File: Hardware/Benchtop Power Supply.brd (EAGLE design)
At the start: 114.3 x 48.3 mm, 20 parts, among them J1 ATX24RH

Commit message: Midway hardware changes
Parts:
- added FRAME1: FRAME-LETTER, SparkFun-Aesthetics:CREATIVE_COMMONS
- added S9: (no value), SparkFun-Electromechanical:SWITCH-SPDT_KIT
- added U$1: REVISION, SparkFun-Aesthetics:REVISION
- J1: device SparkFun:ATX24_RIGHT_ANGLE -> SparkFun-Connectors:ATX24_RIGHT_ANGLE
- moved JP1 84.8 mm to (3.94, 15.6)
- moved S8 21.6 mm to (123.2, 38.1)
- moved F4 19.0 mm to (114.3, 26.7)
- moved JP2 17.8 mm to (129.5, 2.54)
- moved JP3 17.8 mm to (129.5, 45.7)
- moved S6 15.2 mm to (91.4, 38.1)
- moved S7 15.2 mm to (104.1, 38.1)
- moved F3 12.7 mm to (82.5, 26.7)
- moved J1 8.89 mm to (66.0, 8.89)
- moved S4 8.89 mm to (59.7, 38.1)
- moved S5 8.89 mm to (72.4, 38.1)
- moved F1 5.08 mm to (49.5, 26.7)
- moved LED1 3.81 mm to (27.9, 6.35)
- moved R1 3.81 mm to (27.9, 11.4)
- moved S1 3.81 mm to (8.89, 38.1)
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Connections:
- new net N$2: J1.16, S9.2
- net GND: now also S9.3; no longer J1.16
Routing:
- net 3.3V: track 74.7 -> 0.00 mm
- net 5V: track 64.8 -> 0.00 mm
- net 12V: track 31.4 -> 0.00 mm
- net 5V_P: track 15.2 -> 1.35 mm
- net -12V: track 11.0 -> 0.00 mm
- net 3.3V_P: track 9.93 -> 0.95 mm
- net -12V_P: track 8.32 -> 0.00 mm
- net 12V_P: track 8.32 -> 0.00 mm
- net N$1: track 6.13 -> 0.00 mm
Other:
- board size 114.3 x 48.3 mm -> 132.1 x 48.3 mm
- board text added: "Ryan Owens"
- board text added: "Toni Klopfenstein"
- board text added: "V13"
- board text removed: "3/29/10"

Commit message: Files changed for V13- ready for review
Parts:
- added LOGO1: OSHW-LOGOL, SparkFun-Aesthetics:OSHW-LOGO-L
- JP1: value LOGO-SFENEW -> SFE_LOGO_NAME_FLAME.3_INCH; device SparkFun:SFE-NEW-WEBLOGO -> SparkFun-Aesthetics:SFE_LOGO_NAME_FLAME_.3
- moved JP1 93.1 mm to (96.6, 6.73)
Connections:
- new net NC: S9.1
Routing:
- net 3.3V: track 0.00 -> 76.0 mm
- net 5V: track 0.00 -> 67.3 mm
- net N$2: track 0.00 -> 37.2 mm
- net 12V: track 0.00 -> 32.4 mm
- net -12V: track 0.00 -> 22.0 mm
- net 5V_P: track 1.35 -> 18.8 mm
- net 3.3V_P: track 0.95 -> 13.2 mm
- net 12V_P: track 0.00 -> 7.27 mm
- net -12V_P: track 0.00 -> 7.27 mm
- net N$1: track 0.00 -> 6.88 mm
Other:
- board text added: "Off"
- board text added: "On"

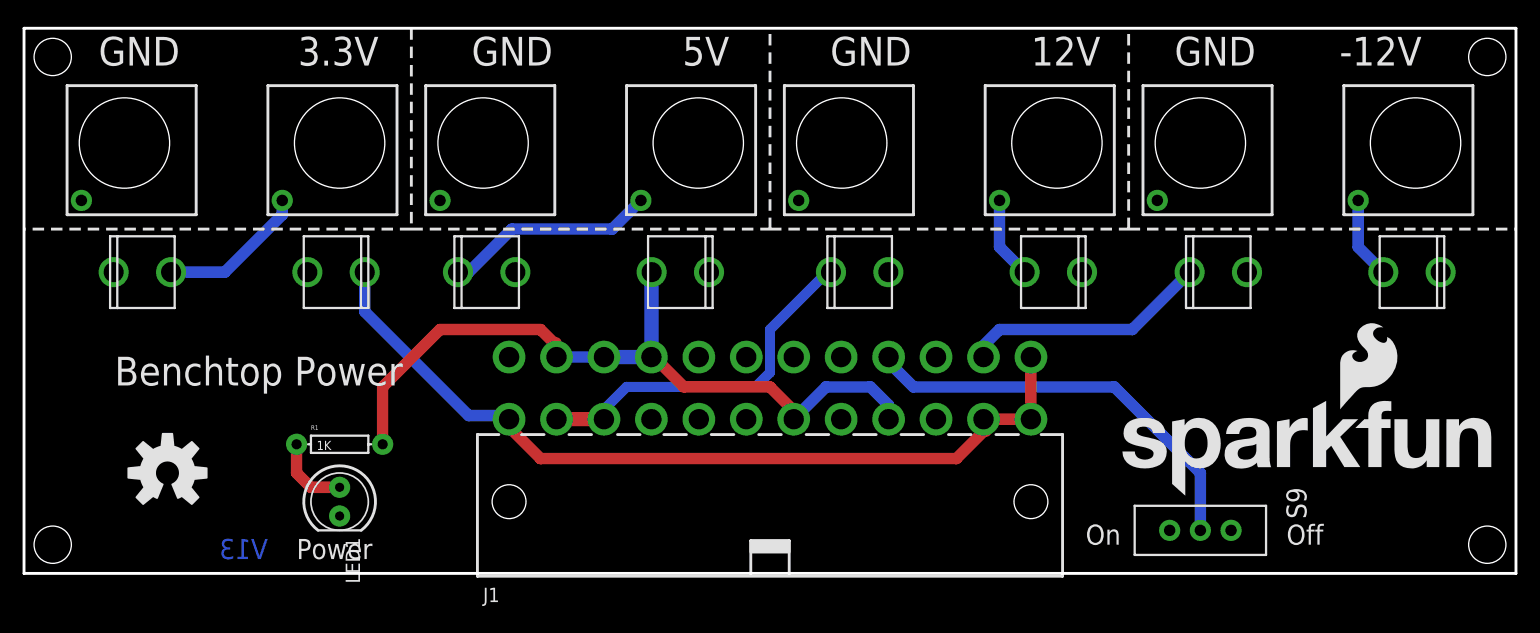
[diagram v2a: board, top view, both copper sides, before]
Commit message: Adding rounded corners, square binding post holes, increased traces to 60 mil
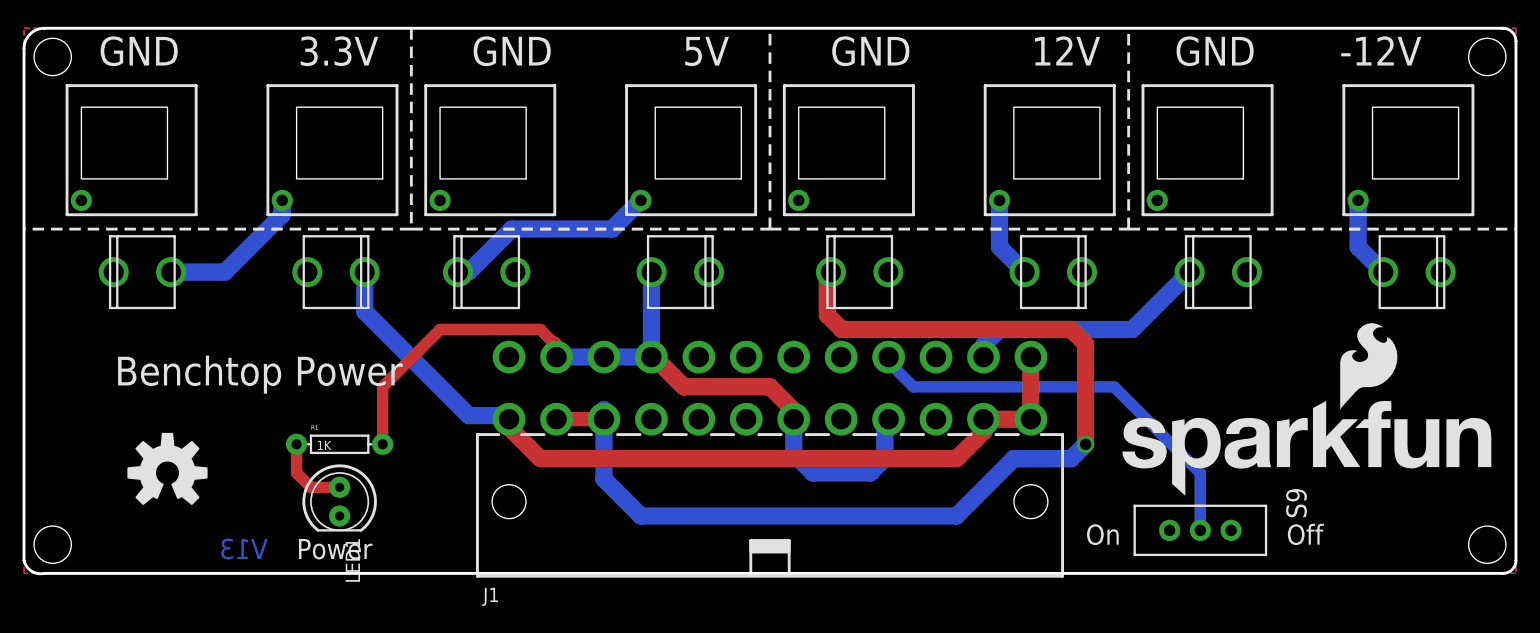
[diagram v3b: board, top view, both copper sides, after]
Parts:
- S1, S2, S3, S4, S5, S6, S7, S8: device SparkFun:BINDING_POST -> SparkFun-Connectors:BINDING_POST
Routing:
- net 12V: track 32.4 -> 95.1 mm, vias 0 -> 1
- net 5V: track 67.3 -> 71.7 mm
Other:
- outline, holes or cut-outs redrawn

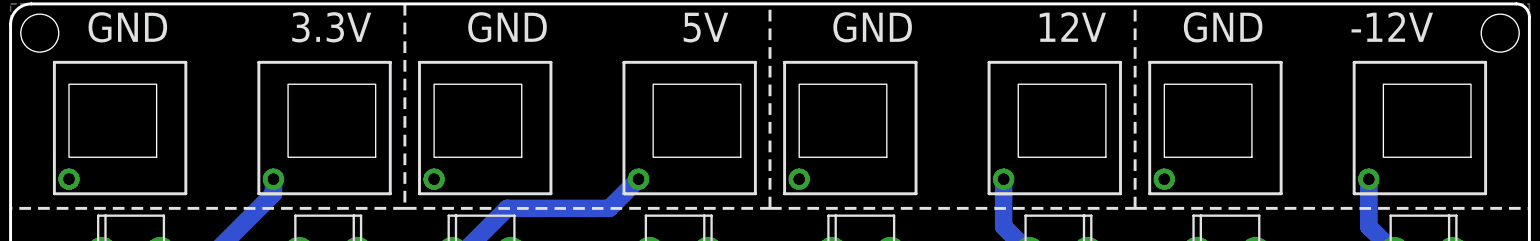
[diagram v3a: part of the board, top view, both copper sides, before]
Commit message: Fixing drill holes for mounting posts
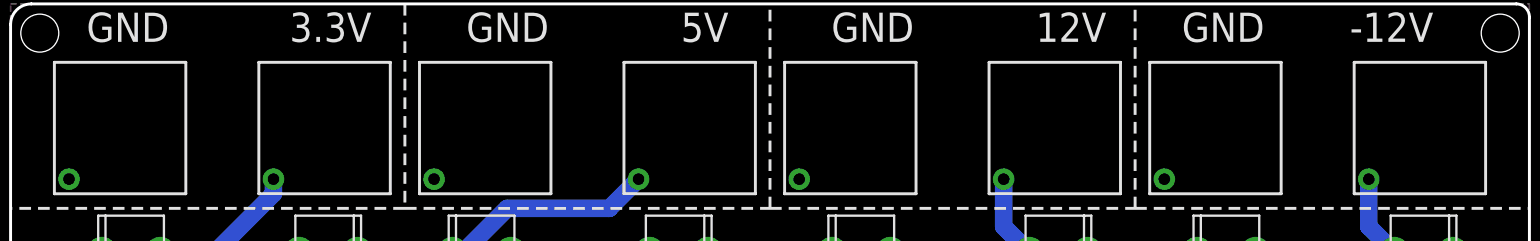
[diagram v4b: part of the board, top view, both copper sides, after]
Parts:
- JP2, JP3, JP4, JP5: device SparkFun:STAND-OFF -> SparkFun-Electromechanical:STAND-OFF
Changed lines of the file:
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@@
 <grid distance="0.05" unitdist="inch" unit="inch" style="lines" multiple="1" display="yes" altdistance="0.005" altunitdist="inch" altunit="inch"/>
 <layers>
-<layer number="1" name="Top" color="4" fill="1" visible="no" active="yes"/>
+<layer number="1" name="Top" color="4" fill="1" visible="yes" active="yes"/>
 <layer number="2" name="Route2" color="1" fill="3" visible="no" active="no"/>
 <layer number="3" name="Route3" color="4" fill="3" visible="no" active="no"/>
@@
 <layer number="14" name="Route14" color="1" fill="6" visible="no" active="no"/>
 <layer number="15" name="Route15" color="4" fill="6" visible="no" active="no"/>
-<layer number="16" name="Bottom" color="1" fill="1" visible="no" active="yes"/>
+<layer number="16" name="Bottom" color="1" fill="1" visible="yes" active="yes"/>
 <layer number="17" name="Pads" color="2" fill="1" visible="yes" active="yes"/>
 <layer number="18" name="Vias" color="2" fill="1" visible="yes" active="yes"/>
@@
 <layer number="46" name="Milling" color="3" fill="1" visible="no" active="yes"/>
 <layer number="47" name="Measures" color="7" fill="1" visible="no" active="yes"/>
-<layer number="48" name="Document" color="7" fill="1" visible="no" active="yes"/>
-<layer number="49" name="Reference" color="7" fill="1" visible="no" active="yes"/>
+<layer number="48" name="Document" color="7" fill="1" visible="yes" active="yes"/>
+<layer number="49" name="Reference" color="7" fill="1" visible="yes" active="yes"/>
 <layer number="50" name="dxf" color="7" fill="1" visible="no" active="yes"/>
 <layer number="51" name="tDocu" color="6" fill="1" visible="yes" active="yes"/>
@@
 <layer number="54" name="bGND_GNDA" color="1" fill="9" visible="no" active="no"/>
 <layer number="56" name="wert" color="7" fill="1" visible="no" active="yes"/>
+<layer number="57" name="tCAD" color="7" fill="1" visible="no" active="no"/>
 <layer number="91" name="Nets" color="2" fill="1" visible="no" active="no"/>
 <layer number="92" name="Busses" color="1" fill="1" visible="no" active="no"/>
@@
 <layer number="97" name="Info" color="7" fill="1" visible="no" active="no"/>
 <layer number="98" name="Guide" color="6" fill="1" visible="no" active="no"/>
+<layer number="99" name="SpiceOrder" color="7" fill="1" visible="no" active="no"/>
 <layer number="100" name="Muster" color="7" fill="1" visible="no" active="no"/>
 <layer number="101" name="Patch_Top" color="12" fill="4" visible="no" active="yes"/>
@@
 <layer number="132" name="bAdjust" color="7" fill="1" visible="no" active="yes"/>
 <layer number="144" name="Drill_legend" color="7" fill="1" visible="no" active="yes"/>
+<layer number="150" name="Notes" color="7" fill="1" visible="yes" active="yes"/>
 <layer number="151" name="HeatSink" color="7" fill="1" visible="no" active="yes"/>
 <layer number="152" name="_bDocu" color="7" fill="1" visible="no" active="yes"/>
+<layer number="153" name="FabDoc1" color="7" fill="1" visible="yes" active="yes"/>
+<layer number="154" name="FabDoc2" color="7" fill="1" visible="yes" active="yes"/>
+<layer number="155" name="FabDoc3" color="7" fill="1" visible="yes" active="yes"/>
 <layer number="199" name="Contour" color="7" fill="1" visible="no" active="yes"/>
 <layer number="200" name="200bmp" color="1" fill="10" visible="no" active="yes"/>
@@
 <elements>
 <element name="JP1" library="SparkFun-Aesthetics" package="SFE_LOGO_NAME_FLAME_.3" value="SFE_LOGO_NAME_FLAME.3_INCH" x="96.647" y="6.731"/>
-<element name="JP2" library="SparkFun" package="STAND-OFF" value="STAND-OFF" x="129.54" y="2.54"/>
-<element name="JP3" library="SparkFun" package="STAND-OFF" value="STAND-OFF" x="129.54" y="45.72"/>
-<element name="JP4" library="SparkFun" package="STAND-OFF" value="STAND-OFF" x="2.54" y="2.54"/>
-<element name="JP5" library="SparkFun" package="STAND-OFF" value="STAND-OFF" x="2.54" y="45.72"/>
+<element name="JP2" library="SparkFun-Electromechanical" package="STAND-OFF" value="STAND-OFF" x="129.54" y="2.54"/>
+<element name="JP3" library="SparkFun-Electromechanical" package="STAND-OFF" value="STAND-OFF" x="129.54" y="45.72"/>
+<element name="JP4" library="SparkFun-Electromechanical" package="STAND-OFF" value="STAND-OFF" x="2.54" y="2.54"/>
+<element name="JP5" library="SparkFun-Electromechanical" package="STAND-OFF" value="STAND-OFF" x="2.54" y="45.72"/>
 <element name="J1" library="SparkFun-Connectors" package="ATX24_RIGHT_ANGLE" value="ATX24RH" x="66.04" y="8.89"/>
 <element name="F1" library="SparkFun" package="FUSE_5MM" value="FUSEX20MM" x="49.53" y="26.67" rot="R270"/>

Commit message: Updating to new binding post footprint
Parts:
- turned S1 to 225 degrees
- turned S2 to 135 degrees
- turned S3 to 225 degrees
- turned S4 to 135 degrees
- turned S5 to 225 degrees
- turned S6 to 135 degrees
- turned S7 to 225 degrees
- turned S8 to 135 degrees
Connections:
- net -12V_P: now also S8.P$1
- net 12V_P: now also S6.P$1
- net 3.3V_P: now also S2.P$1
- net 5V_P: now also S4.P$1
- net GND: now also S1.P$1, S3.P$1, S5.P$1, S7.P$1
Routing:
- net 3.3V_P: track 13.2 -> 13.7 mm, vias 1 -> 0
- net 12V_P: track 7.27 -> 7.71 mm, vias 1 -> 0
- net -12V_P: track 7.27 -> 7.71 mm, vias 1 -> 0
- net 5V_P: vias 1 -> 0
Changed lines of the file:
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@@
 <layer number="46" name="Milling" color="3" fill="1" visible="no" active="yes"/>
 <layer number="47" name="Measures" color="7" fill="1" visible="no" active="yes"/>
-<layer number="48" name="Document" color="7" fill="1" visible="yes" active="yes"/>
-<layer number="49" name="Reference" color="7" fill="1" visible="yes" active="yes"/>
+<layer number="48" name="Document" color="7" fill="1" visible="no" active="yes"/>
+<layer number="49" name="Reference" color="7" fill="1" visible="no" active="yes"/>
 <layer number="50" name="dxf" color="7" fill="1" visible="no" active="yes"/>
 <layer number="51" name="tDocu" color="6" fill="1" visible="yes" active="yes"/>
@@
 <layer number="132" name="bAdjust" color="7" fill="1" visible="no" active="yes"/>
 <layer number="144" name="Drill_legend" color="7" fill="1" visible="no" active="yes"/>
-<layer number="150" name="Notes" color="7" fill="1" visible="yes" active="yes"/>
+<layer number="150" name="Notes" color="7" fill="1" visible="no" active="yes"/>
 <layer number="151" name="HeatSink" color="7" fill="1" visible="no" active="yes"/>
 <layer number="152" name="_bDocu" color="7" fill="1" visible="no" active="yes"/>
-<layer number="153" name="FabDoc1" color="7" fill="1" visible="yes" active="yes"/>
-<layer number="154" name="FabDoc2" color="7" fill="1" visible="yes" active="yes"/>
-<layer number="155" name="FabDoc3" color="7" fill="1" visible="yes" active="yes"/>
+<layer number="153" name="FabDoc1" color="7" fill="1" visible="no" active="yes"/>
+<layer number="154" name="FabDoc2" color="7" fill="1" visible="no" active="yes"/>
+<layer number="155" name="FabDoc3" color="7" fill="1" visible="no" active="yes"/>
 <layer number="199" name="Contour" color="7" fill="1" visible="no" active="yes"/>
 <layer number="200" name="200bmp" color="1" fill="10" visible="no" active="yes"/>
@@
 </class>
 </classes>
-<designrules name="SparkFun *">
+<designrules name="SparkFun-2-layer">
 <description language="en">&lt;b&gt;EAGLE Design Rules&lt;/b&gt;
 &lt;p&gt;
@@
 <param name="mdDrill" value="8mil"/>
 <param name="mdSmdStop" value="0mil"/>
-<param name="msWidth" value="8mil"/>
-<param name="msDrill" value="20mil"/>
+<param name="msWidth" value="7mil"/>
+<param name="msDrill" value="15mil"/>
 <param name="msMicroVia" value="9.99mm"/>
 <param name="msBlindViaRatio" value="0.5"/>
@@
 <element name="R1" library="SparkFun" package="AXIAL-0.3" value="1K" x="27.94" y="11.43"/>
 <element name="LED1" library="SparkFun" package="LED5MM" value="RED" x="27.94" y="6.35" rot="R270"/>
-<element name="S1" library="SparkFun-Connectors" package="BINDING_POST" value="BINDING_POST" x="8.89" y="38.1" rot="R90"/>
-<element name="S2" library="SparkFun-Connectors" package="BINDING_POST" value="BINDING_POST" x="27.94" y="38.1" rot="R90"/>
-<element name="S3" library="SparkFun-Connectors" package="BINDING_POST" value="BINDING_POST" x="40.64" y="38.1" rot="R90"/>
-<element name="S4" library="SparkFun-Connectors" package="BINDING_POST" value="BINDING_POST" x="59.69" y="38.1" rot="R90"/>
-<element name="S5" library="SparkFun-Connectors" package="BINDING_POST" value="BINDING_POST" x="72.39" y="38.1" rot="R90"/>
-<element name="S6" library="SparkFun-Connectors" package="BINDING_POST" value="BINDING_POST" x="91.44" y="38.1" rot="R90"/>
-<element name="S7" library="SparkFun-Connectors" package="BINDING_POST" value="BINDING_POST" x="104.14" y="38.1" rot="R90"/>
-<element name="S8" library="SparkFun-Connectors" package="BINDING_POST" value="BINDING_POST" x="123.19" y="38.1" rot="R90"/>
+<element name="S1" library="SparkFun-Connectors" package="BINDING_POST" value="BINDING_POST" x="8.89" y="38.1" rot="R225"/>
+<element name="S2" library="SparkFun-Connectors" package="BINDING_POST" value="BINDING_POST" x="27.94" y="38.1" rot="R135"/>
+<element name="S3" library="SparkFun-Connectors" package="BINDING_POST" value="BINDING_POST" x="40.64" y="38.1" rot="R225"/>
+<element name="S4" library="SparkFun-Connectors" package="BINDING_POST" value="BINDING_POST" x="59.69" y="38.1" rot="R135"/>
+<element name="S5" library="SparkFun-Connectors" package="BINDING_POST" value="BINDING_POST" x="72.39" y="38.1" rot="R225"/>
+<element name="S6" library="SparkFun-Connectors" package="BINDING_POST" value="BINDING_POST" x="91.44" y="38.1" rot="R135"/>
+<element name="S7" library="SparkFun-Connectors" package="BINDING_POST" value="BINDING_POST" x="104.14" y="38.1" rot="R225"/>
+<element name="S8" library="SparkFun-Connectors" package="BINDING_POST" value="BINDING_POST" x="123.19" y="38.1" rot="R135"/>
 <element name="S9" library="SparkFun-Electromechanical" package="SWITCH-SPDT_KIT" value="" x="104.14" y="3.81" rot="R270">
 <attribute name="PROD_ID" value="SWCH-08261" x="104.14" y="3.81" size="1.778" layer="27" font="vector" ratio="15" rot="R270" display="off"/>
@@
 <contactref element="J1" pad="24"/>
 <contactref element="LED1" pad="K"/>
-<via x="5.08" y="33.02" extent="1-16" drill="1.016" diameter="1.8796"/>
-<via x="36.83" y="33.02" extent="1-16" drill="1.016" diameter="1.8796"/>
-<via x="68.58" y="33.02" extent="1-16" drill="1.016" diameter="1.8796"/>
-<via x="100.33" y="33.02" extent="1-16" drill="1.016" diameter="1.8796"/>
 <polygon width="0.254" layer="16" isolate="0.3048">
 <vertex x="0" y="0"/>
@@
 </polygon>
 <contactref element="S9" pad="3"/>
+<contactref element="S7" pad="P$1"/>
+<contactref element="S1" pad="P$1"/>
+<contactref element="S3" pad="P$1"/>
+<contactref element="S5" pad="P$1"/>
 </signal>
 <signal name="5V">
@@
 <signal name="5V_P">
 <contactref element="F1" pad="1"/>
-<via x="54.61" y="33.02" extent="1-16" drill="1.016" diameter="1.8796"/>
 <wire x1="38.4175" y1="26.67" x2="39.37" y2="26.67" width="1.016" layer="16"/>
 <wire x1="39.37" y1="26.67" x2="43.18" y2="30.48" width="1.524" layer="16"/>
 <wire x1="43.18" y1="30.48" x2="52.07" y2="30.48" width="1.524" layer="16"/>
-<wire x1="52.07" y1="30.48" x2="54.61" y2="33.02" width="1.524" layer="16"/>
+<wire x1="52.07" y1="30.48" x2="54.30184375" y2="32.71184375" width="1.524" layer="16"/>
+<contactref element="S4" pad="P$1"/>
+<wire x1="54.30184375" y1="32.71184375" x2="54.61" y2="33.02" width="1.524" layer="16"/>
 </signal>
 <signal name="3.3V_P">
 <contactref element="F2" pad="3"/>
-<via x="22.86" y="33.02" extent="1-16" drill="1.016" diameter="1.8796"/>
 <wire x1="22.86" y1="33.02" x2="22.86" y2="31.75" width="1.524" layer="16"/>
 <wire x1="22.86" y1="31.75" x2="17.78" y2="26.67" width="1.524" layer="16"/>
 <wire x1="17.78" y1="26.67" x2="13.0175" y2="26.67" width="1.524" layer="16"/>
+<contactref element="S2" pad="P$1"/>
+<wire x1="22.55184375" y1="32.71184375" x2="22.86" y2="33.02" width="1.524" layer="16"/>
 </signal>
 <signal name="12V_P">
 <contactref element="F3" pad="3"/>
-<via x="86.36" y="33.02" extent="1-16" drill="1.016" diameter="1.8796"/>
 <wire x1="86.36" y1="33.02" x2="86.36" y2="28.8925" width="1.524" layer="16"/>
 <wire x1="86.36" y1="28.8925" x2="88.5825" y2="26.67" width="1.524" layer="16"/>
+<contactref element="S6" pad="P$1"/>
+<wire x1="86.05184375" y1="32.71184375" x2="86.36" y2="33.02" width="1.524" layer="16"/>
 </signal>
 <signal name="-12V_P">
 <contactref element="F4" pad="3"/>
-<via x="118.11" y="33.02" extent="1-16" drill="1.016" diameter="1.8796"/>
 <wire x1="118.11" y1="33.02" x2="118.11" y2="28.8925" width="1.524" layer="16"/>
 <wire x1="118.11" y1="28.8925" x2="120.3325" y2="26.67" width="1.524" layer="16"/>
+<contactref element="S8" pad="P$1"/>
+<wire x1="118.11" y1="33.02" x2="117.80184375" y2="32.71184375" width="1.524" layer="16"/>
 </signal>
 <signal name="N$1">
